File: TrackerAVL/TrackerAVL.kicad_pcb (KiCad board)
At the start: 2 copper layers, 120 x 80 mm, 173 parts, among them J801 Conn_02x07_Odd_Even, J802 Conn_01x15, J803 Conn_01x04, P201 uC_debug, Q201 DTC043ZEBTL, Q202 DTC043ZEBTL, Q203 DTC043ZEBTL, Q701 2N7002P, Q702 2N7002P, Q703 2N7002P, Q704 DTC043ZEBTL, U201 MAX3221, U202 LPC4337JBD144, U203 STS8C5H30L, U301 MPU-6050, U401 NAU8814, U501 STS8C5H30L, U502 LD1085D2T33R, U503 NCP114ASN180T1G, U601 MPCIE-Socket, U701 74LVC244APW, U801 74HC4053, X201 12MHz, X202 32.768K

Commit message: Cambios en pcb
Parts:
- moved C304 2.90 mm to (91.5, 36.8), turned to 0 degrees
- moved C303 1.94 mm to (79.6, 34.5)
- moved C301 1.91 mm to (79.6, 36.5)
- moved C401 1.58 mm to (134.9, 53.2)
- moved C402 1.56 mm to (134.9, 55.3)
- moved C403 1.55 mm to (134.9, 57.4)
- moved C404 1.51 mm to (134.9, 59.4)
- moved R406 1.15 mm to (149.2, 53.0)
- moved R408 1.13 mm to (149.2, 55.0)
- moved R407 1.13 mm to (149.2, 57.1)
- moved JP401 0.73 mm to (149.2, 49.1)
- moved C302 0.45 mm to (81.4, 30.2)
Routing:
- net /Audio/MICBIAS: track 25.4 -> 54.4 mm
- net +3V3: track 620.1 -> 641.9 mm, vias 78 -> 77
- net GND: track 487.1 -> 496.8 mm, vias 61 -> 60
- net /VBAT: track 102.5 -> 93.2 mm
- net +1V8: track 115.1 -> 121.7 mm
- net /Acelerómetro/INT: track 23.4 -> 27.4 mm
- net +BATT: track 13.0 -> 10.4 mm
- net Net-(R406-Pad1): track 4.71 -> 7.06 mm
- net Net-(C303-Pad1): track 2.49 -> 4.49 mm
- net /UC20_PCIe/I2C_SDA: track 38.9 -> 40.8 mm
- net /I2C_SCL: track 56.7 -> 58.5 mm
- net Net-(R403-Pad1): track 3.67 -> 5.38 mm
- net /I2C_SDA: track 59.6 -> 61.1 mm
- net Net-(R401-Pad1): track 3.96 -> 5.26 mm
- net /Audio/MICP: track 5.06 -> 6.22 mm
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
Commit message: Cambios en pcb
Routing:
- net GND: track 496.8 -> 497.7 mm, vias 60 -> 61

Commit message: Cambios en pcb
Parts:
- JP401: footprint Jumper:SolderJumper-2_P1.3mm_Bridged_Pad1.0x1.5mm -> NetTie:NetTie-2_SMD_Pad0.5mm
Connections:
- P201 pad 7: Net-(P201-Pad7) -> (no net)
- U201 pad 10: Net-(U201-Pad10) -> (no net)
- U202 pad 1: Net-(U202-Pad1) -> (no net)
- U202 pad 10: Net-(U202-Pad10) -> (no net)
- U202 pad 102: Net-(U202-Pad102) -> (no net)
- U202 pad 108: Net-(U202-Pad108) -> (no net)
- U202 pad 11: Net-(U202-Pad11) -> (no net)
- U202 pad 110: Net-(U202-Pad110) -> (no net)
- U202 pad 112: Net-(U202-Pad112) -> (no net)
- U202 pad 114: Net-(U202-Pad114) -> (no net)
- U202 pad 116: Net-(U202-Pad116) -> (no net)
- U202 pad 117: Net-(U202-Pad117) -> (no net)
- U202 pad 118: Net-(U202-Pad118) -> (no net)
- U202 pad 119: Net-(U202-Pad119) -> (no net)
- U202 pad 121: Net-(U202-Pad121) -> (no net)
- U202 pad 122: Net-(U202-Pad122) -> (no net)
- U202 pad 123: Net-(U202-Pad123) -> (no net)
- U202 pad 124: Net-(U202-Pad124) -> (no net)
- U202 pad 127: Net-(U202-Pad127) -> (no net)
- U202 pad 129: Net-(U202-Pad129) -> (no net)
- U202 pad 130: Net-(U202-Pad130) -> (no net)
- U202 pad 132: Net-(U202-Pad132) -> (no net)
- U202 pad 133: Net-(U202-Pad133) -> (no net)
- U202 pad 134: Net-(U202-Pad134) -> (no net)
- U202 pad 136: Net-(U202-Pad136) -> (no net)
- U202 pad 14: Net-(U202-Pad14) -> (no net)
- U202 pad 140: Net-(U202-Pad140) -> (no net)
- U202 pad 142: Net-(U202-Pad142) -> (no net)
- U202 pad 144: Net-(U202-Pad144) -> (no net)
- U202 pad 15: Net-(U202-Pad15) -> (no net)
- U202 pad 18: Net-(U202-Pad18) -> (no net)
- U202 pad 20: Net-(U202-Pad20) -> (no net)
- U202 pad 21: Net-(U202-Pad21) -> (no net)
- U202 pad 22: Net-(U202-Pad22) -> (no net)
- U202 pad 24: Net-(U202-Pad24) -> (no net)
- U202 pad 3: Net-(U202-Pad3) -> (no net)
- U202 pad 32: Net-(U202-Pad32) -> (no net)
- U202 pad 33: Net-(U202-Pad33) -> (no net)
- U202 pad 34: Net-(U202-Pad34) -> (no net)
- U202 pad 35: Net-(U202-Pad35) -> (no net)
- U202 pad 37: Net-(U202-Pad37) -> (no net)
- U202 pad 39: Net-(U202-Pad39) -> (no net)
- U202 pad 44: Net-(U202-Pad44) -> (no net)
- U202 pad 45: Net-(U202-Pad45) -> (no net)
- U202 pad 46: Net-(U202-Pad46) -> (no net)
- U202 pad 48: Net-(U202-Pad48) -> (no net)
- U202 pad 50: Net-(U202-Pad50) -> (no net)
- U202 pad 51: Net-(U202-Pad51) -> (no net)
- U202 pad 52: Net-(U202-Pad52) -> (no net)
- U202 pad 53: Net-(U202-Pad53) -> (no net)
- U202 pad 54: Net-(U202-Pad54) -> (no net)
- U202 pad 55: Net-(U202-Pad55) -> (no net)
- U202 pad 56: Net-(U202-Pad56) -> (no net)
- U202 pad 57: Net-(U202-Pad57) -> (no net)
- U202 pad 58: Net-(U202-Pad58) -> (no net)
- U202 pad 6: Net-(U202-Pad6) -> (no net)
- U202 pad 60: Net-(U202-Pad60) -> (no net)
- U202 pad 61: Net-(U202-Pad61) -> (no net)
- U202 pad 62: Net-(U202-Pad62) -> (no net)
- U202 pad 63: Net-(U202-Pad63) -> (no net)
- U202 pad 64: Net-(U202-Pad64) -> (no net)
- U202 pad 65: Net-(U202-Pad65) -> (no net)
- U202 pad 66: Net-(U202-Pad66) -> (no net)
- U202 pad 67: Net-(U202-Pad67) -> (no net)
- U202 pad 68: Net-(U202-Pad68) -> (no net)
- U202 pad 69: Net-(U202-Pad69) -> (no net)
- U202 pad 7: Net-(U202-Pad7) -> (no net)
- U202 pad 70: Net-(U202-Pad70) -> (no net)
- U202 pad 72: Net-(U202-Pad72) -> (no net)
- U202 pad 73: Net-(U202-Pad73) -> (no net)
- U202 pad 78: Net-(U202-Pad78) -> (no net)
- U202 pad 79: Net-(U202-Pad79) -> (no net)
- U202 pad 8: Net-(U202-Pad8) -> (no net)
- U202 pad 83: Net-(U202-Pad83) -> (no net)
- U202 pad 89: Net-(U202-Pad89) -> (no net)
- U202 pad 9: Net-(U202-Pad9) -> (no net)
- U202 pad 90: Net-(U202-Pad90) -> (no net)
- U202 pad 98: Net-(U202-Pad98) -> (no net)
- U202 pad 99: Net-(U202-Pad99) -> (no net)
- U301 pad 6: Net-(U301-Pad6) -> (no net)
- U301 pad 7: Net-(U301-Pad7) -> (no net)
- U401 pad 16: Net-(U401-Pad16) -> (no net)
- U401 pad 21: Net-(U401-Pad21) -> (no net)
- U601 pad 1: Net-(U601-Pad1) -> (no net)
- U601 pad 10: Net-(U601-Pad10) -> (no net)
- U601 pad 12: Net-(U601-Pad12) -> (no net)
- U601 pad 14: Net-(U601-Pad14) -> (no net)
- U601 pad 16: Net-(U601-Pad16) -> (no net)
- U601 pad 17: Net-(U601-Pad17) -> (no net)
- U601 pad 19: Net-(U601-Pad19) -> (no net)
- U601 pad 23: Net-(U601-Pad23) -> (no net)
- U601 pad 24: Net-(U601-Pad24) -> (no net)
- U601 pad 25: Net-(U601-Pad25) -> (no net)
- U601 pad 28: Net-(U601-Pad28) -> (no net)
- U601 pad 3: Net-(U601-Pad3) -> (no net)
- U601 pad 33: Net-(U601-Pad33) -> (no net)
- U601 pad 36: Net-(U601-Pad36) -> (no net)
- U601 pad 38: Net-(U601-Pad38) -> (no net)
- U601 pad 42: Net-(U601-Pad42) -> (no net)
- U601 pad 44: Net-(U601-Pad44) -> (no net)
- U601 pad 46: Net-(U601-Pad46) -> (no net)
- U601 pad 48: Net-(U601-Pad48) -> (no net)
- U601 pad 5: Net-(U601-Pad5) -> (no net)
- U601 pad 6: Net-(U601-Pad6) -> (no net)
- U601 pad 7: Net-(U601-Pad7) -> (no net)
- U601 pad 8: Net-(U601-Pad8) -> (no net)
- U701 pad 12: Net-(U701-Pad12) -> (no net)
- U701 pad 8: Net-(U701-Pad8) -> (no net)
- U801 pad 5: Net-(U801-Pad5) -> (no net)

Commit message: Últimos cambios en pcb
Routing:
- net GND: track 497.7 -> 495.1 mm, vias 61 -> 59
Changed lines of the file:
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@@
     (thickness 1.6)
     (drawings 30)
-    (tracks 2672)
+    (tracks 2670)
     (zones 0)
     (modules 173)
@@
   )
   (setup
-    (last_trace_width 0.25)
+    (last_trace_width 0.5)
     (user_trace_width 0.2)
     (user_trace_width 0.24)
@@
   (segment (start 101.475 67.275) (end 100.6 68.15) (width 0.25) (layer F.Cu) (net 1))
   (segment (start 100.6 71.125) (end 101.7 71.125) (width 0.5) (layer F.Cu) (net 1))
-  (segment (start 124.5 61.375) (end 124.5 59.22) (width 0.5) (layer F.Cu) (net 1))
+  (segment (start 124.5 61.375) (end 124.5 59.22) (width 0.25) (layer F.Cu) (net 1))
   (segment (start 121.475 69.355) (end 120.205 69.355) (width 0.5) (layer F.Cu) (net 1))
   (segment (start 121.475 67.85) (end 121.475 69.355) (width 0.5) (layer F.Cu) (net 1))
@@
   (via (at 120.5 43.55) (size 0.8) (drill 0.4) (layers F.Cu B.Cu) (net 1))
   (segment (start 120.5 45.15) (end 120.5 43.55) (width 0.5) (layer F.Cu) (net 1))
-  (via (at 149.1 61.25) (size 0.8) (drill 0.4) (layers F.Cu B.Cu) (net 1))
   (segment (start 149.1 59.275) (end 149.125 59.25) (width 0.5) (layer F.Cu) (net 1))
   (segment (start 149.1 61.25) (end 149.1 59.275) (width 0.5) (layer F.Cu) (net 1))
@@
   (segment (start 87.8 86.825) (end 90.875 86.825) (width 0.75) (layer F.Cu) (net 1))
   (via (at 133.9 61) (size 0.8) (drill 0.4) (layers F.Cu B.Cu) (net 1))
-  (via (at 149.9 51.425004) (size 0.8) (drill 0.4) (layers F.Cu B.Cu) (net 1))
-  (segment (start 149.9 51.990689) (end 149.9 51.425004) (width 0.5) (layer F.Cu) (net 1))
-  (segment (start 149.75 53.075) (end 149.9 52.925) (width 0.5) (layer F.Cu) (net 1))
-  (segment (start 149.9 52.925) (end 149.9 51.990689) (width 0.5) (layer F.Cu) (net 1))
-  (via (at 156.325 51.425) (size 0.8) (drill 0.4) (layers F.Cu B.Cu) (net 1))
-  (segment (start 149.9 51.425004) (end 156.324996 51.425004) (width 0.5) (layer B.Cu) (net 1))
-  (segment (start 156.324996 51.425004) (end 156.325 51.425) (width 0.5) (layer B.Cu) (net 1))
-  (via (at 156.3 61.225) (size 0.8) (drill 0.4) (layers F.Cu B.Cu) (net 1))
-  (segment (start 149.1 61.25) (end 156.275 61.25) (width 0.5) (layer B.Cu) (net 1))
-  (segment (start 156.275 61.25) (end 156.3 61.225) (width 0.5) (layer B.Cu) (net 1))
-  (segment (start 156.325 61.2) (end 156.3 61.225) (width 0.5) (layer F.Cu) (net 1))
-  (segment (start 156.325 51.425) (end 156.325 61.2) (width 0.5) (layer F.Cu) (net 1))
-  (segment (start 149.25 50.775004) (end 149.9 51.425004) (width 0.25) (layer F.Cu) (net 1))
-  (segment (start 149.25 49.8) (end 149.25 50.775004) (width 0.25) (layer F.Cu) (net 1))
   (segment (start 82.61486 34.58514) (end 82.324999 34.875001) (width 0.25) (layer F.Cu) (net 1))
   (segment (start 82.324999 34.875001) (end 81.925 35.275) (width 0.25) (layer F.Cu) (net 1))
@@
   (via (at 93.148372 35.15) (size 0.8) (drill 0.4) (layers F.Cu B.Cu) (net 1))
   (via (at 90.275 31.75) (size 0.8) (drill 0.4) (layers F.Cu B.Cu) (net 1))
+  (segment (start 55.2 61.55) (end 58.75 58) (width 0.5) (layer F.Cu) (net 1))
+  (segment (start 51.45 61.55) (end 55.2 61.55) (width 0.5) (layer F.Cu) (net 1))
+  (segment (start 149.875002 51.025001) (end 150.275001 51.425) (width 0.25) (layer F.Cu) (net 1))
+  (segment (start 149.25 50.399999) (end 149.875002 51.025001) (width 0.25) (layer F.Cu) (net 1))
+  (segment (start 149.25 49.8) (end 149.25 50.399999) (width 0.25) (layer F.Cu) (net 1))
+  (segment (start 150.225 51.475001) (end 150.275001 51.425) (width 0.5) (layer F.Cu) (net 1))
+  (segment (start 150.225 53.025) (end 150.225 51.475001) (width 0.5) (layer F.Cu) (net 1))
+  (via (at 150.275001 51.425) (size 0.8) (drill 0.4) (layers F.Cu B.Cu) (net 1))
+  (via (at 149.1 61.25) (size 0.8) (drill 0.4) (layers F.Cu B.Cu) (net 1))
+  (segment (start 150.675 51.824999) (end 150.275001 51.425) (width 0.5) (layer B.Cu) (net 1))
+  (segment (start 152.325001 53.475) (end 150.675 51.824999) (width 0.5) (layer B.Cu) (net 1))
+  (segment (start 152.325001 58.024999) (end 152.325001 53.475) (width 0.5) (layer B.Cu) (net 1))
+  (segment (start 149.1 61.25) (end 152.325001 58.024999) (width 0.5) (layer B.Cu) (net 1))
   (via (at 73 82) (size 0.8) (drill 0.4) (layers F.Cu B.Cu) (net 2))
   (via (at 71 82) (size 0.8) (drill 0.4) (layers F.Cu B.Cu) (net 2))
@@
   (via (at 90.90093 61.50093) (size 0.8) (drill 0.4) (layers F.Cu B.Cu) (net 15))
   (segment (start 90.90093 60.958216) (end 90.90093 61.50093) (width 0.24) (layer B.Cu) (net 15))
-  (segment (start 122.45 61.375) (end 120.5 61.375) (width 0.5) (layer F.Cu) (net 16))
+  (segment (start 122.45 61.375) (end 120.5 61.375) (width 0.25) (layer F.Cu) (net 16))
   (segment (start 116.7 60.3) (end 115.9 59.5) (width 0.25) (layer F.Cu) (net 16))
   (segment (start 120.5 60.3) (end 116.7 60.3) (width 0.25) (layer F.Cu) (net 16))
@@
   (segment (start 69.3 60) (end 69.1 59.8) (width 0.25) (layer F.Cu) (net 16))
   (segment (start 120.5 57.065) (end 122.45 57.065) (width 0.25) (layer F.Cu) (net 17))
-  (segment (start 122.45 57.065) (end 122.45 59.22) (width 0.5) (layer F.Cu) (net 17))
+  (segment (start 122.45 57.065) (end 122.45 59.22) (width 0.25) (layer F.Cu) (net 17))
   (via (at 69.3 61.1) (size 0.8) (drill 0.4) (layers F.Cu B.Cu) (net 17))
   (segment (start 67.925 61.1) (end 69.3 61.1) (width 0.25) (layer F.Cu) (net 17))
@@
   (segment (start 65.85 96.705) (end 62.905 96.705) (width 0.5) (layer F.Cu) (net 107))
   (segment (start 71.25 92.895) (end 71.25 94.165) (width 0.5) (layer F.Cu) (net 107))
-  (segment (start 70.225 94.165) (end 71.25 94.165) (width 0.25) (layer F.Cu) (net 107))
-  (segment (start 68.74 95.65) (end 70.225 94.165) (width 0.25) (layer F.Cu) (net 107))
-  (segment (start 65.85 96.705) (end 66.795 96.705) (width 0.25) (layer F.Cu) (net 107))
-  (segment (start 67.85 95.65) (end 68.74 95.65) (width 0.25) (layer F.Cu) (net 107))
-  (segment (start 66.795 96.705) (end 67.85 95.65) (width 0.25) (layer F.Cu) (net 107))
-  (segment (start 148.9 90.5) (end 150.45 88.95) (width 0.5) (layer F.Cu) (net 108))
-  (segment (start 147.4 90.5) (end 148.9 90.5) (width 0.5) (layer F.Cu) (net 108))
+  (segment (start 70.225 94.165) (end 71.25 94.165) (width 0.5) (layer F.Cu) (net 107))
+  (segment (start 68.74 95.65) (end 70.225 94.165) (width 0.5) (layer F.Cu) (net 107))
+  (segment (start 65.85 96.705) (end 66.795 96.705) (width 0.5) (layer F.Cu) (net 107))
+  (segment (start 67.85 95.65) (end 68.74 95.65) (width 0.5) (layer F.Cu) (net 107))
+  (segment (start 66.795 96.705) (end 67.85 95.65) (width 0.5) (layer F.Cu) (net 107))
+  (segment (start 148.9 90.5) (end 150.45 88.95) (width 0.25) (layer F.Cu) (net 108))
+  (segment (start 147.4 90.5) (end 148.9 90.5) (width 0.25) (layer F.Cu) (net 108))
   (via (at 150.4 80) (size 0.8) (drill 0.4) (layers F.Cu B.Cu) (net 108))
-  (segment (start 150.45 88.95) (end 150.45 80.05) (width 0.5) (layer F.Cu) (net 108))
+  (segment (start 150.45 88.95) (end 150.45 80.05) (width 0.25) (layer F.Cu) (net 108))
   (segment (start 150.45 80.05) (end 150.4 80) (width 0.5) (layer F.Cu) (net 108))
-  (segment (start 150.4 80) (end 149.9 79.5) (width 0.5) (layer B.Cu) (net 108))
+  (segment (start 150.4 80) (end 149.9 79.5) (width 0.25) (layer B.Cu) (net 108))
   (via (at 149.9 75.45) (size 0.8) (drill 0.4) (layers F.Cu B.Cu) (net 108))
-  (segment (start 149.9 79.5) (end 149.9 75.45) (width 0.5) (layer B.Cu) (net 108))
-  (segment (start 149.9 75.45) (end 149.9 72) (width 0.5) (layer F.Cu) (net 108))
-  (segment (start 146.875 68.975) (end 145.35 68.975) (width 0.5) (layer F.Cu) (net 108))
-  (segment (start 149.9 72) (end 146.875 68.975) (width 0.5) (layer F.Cu) (net 108))
+  (segment (start 149.9 79.5) (end 149.9 75.45) (width 0.25) (layer B.Cu) (net 108))
+  (segment (start 149.9 75.45) (end 149.9 72) (width 0.25) (layer F.Cu) (net 108))
+  (segment (start 146.875 68.975) (end 145.35 68.975) (width 0.25) (layer F.Cu) (net 108))
+  (segment (start 149.9 72) (end 146.875 68.975) (width 0.25) (layer F.Cu) (net 108))
   (segment (start 62.8 104.275) (end 64.87501 106.35001) (width 0.25) (layer F.Cu) (net 109))
   (segment (start 61.95 104.275) (end 62.8 104.275) (width 0.25) (layer F.Cu) (net 109))

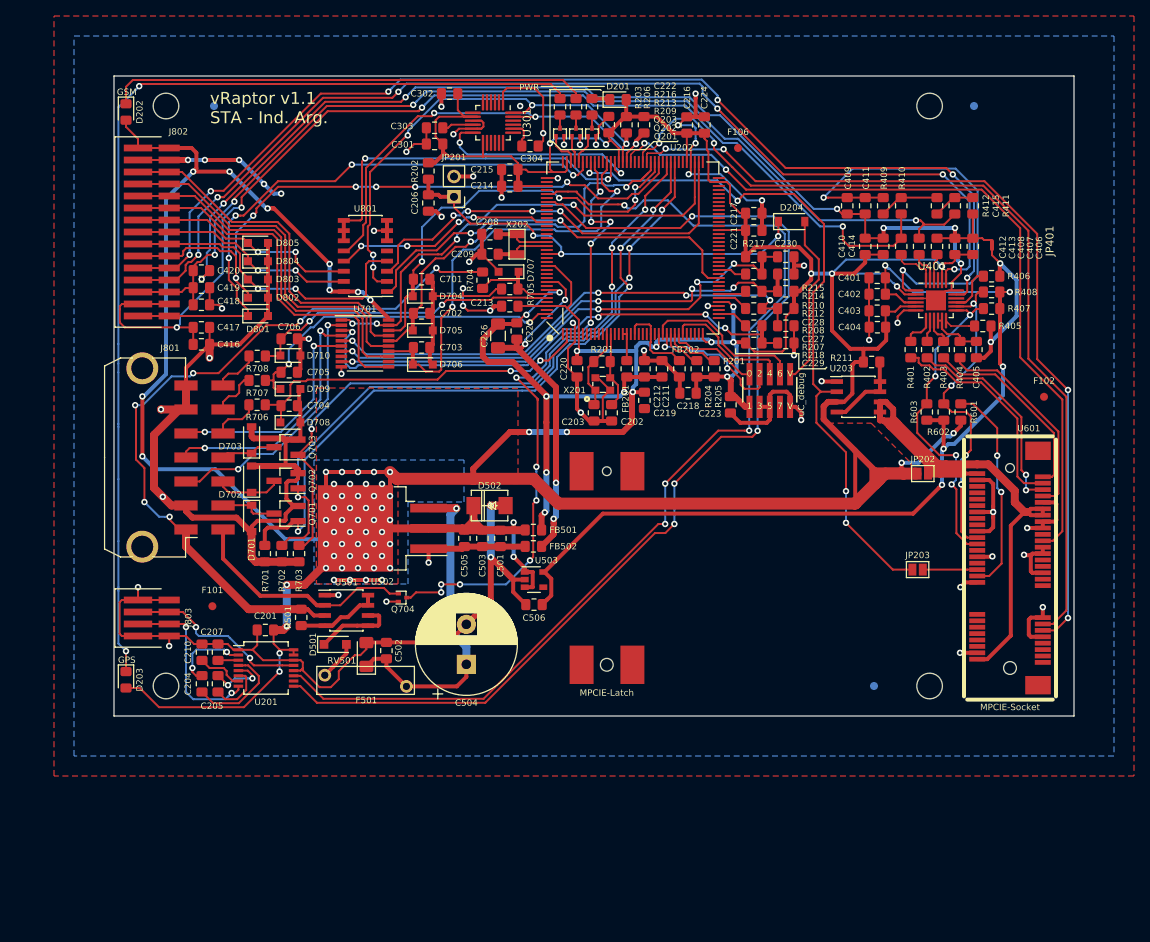
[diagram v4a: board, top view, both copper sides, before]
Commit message: Modificaciones varias
Se modifica acceso de pistas a pads (ahora a 90°).
Se agregan archivos de información al proyecto.
Se corrigen elementos 3d 24-QFN.
Modificaciones varias de pistas.
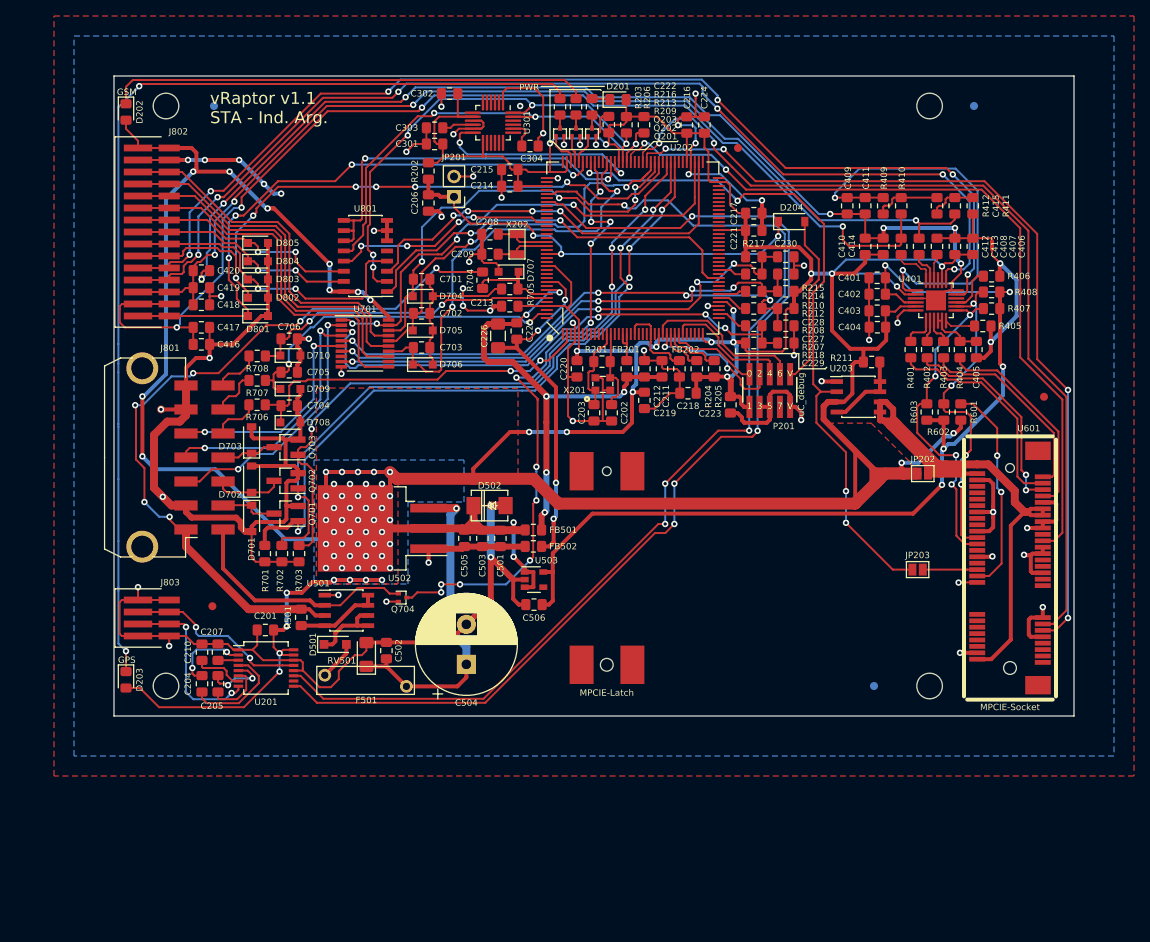
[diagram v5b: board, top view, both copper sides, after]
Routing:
- net GND: track 495.1 -> 507.3 mm
- net /Audio/MICBIAS: track 54.4 -> 51.9 mm
- net /CPU/DISPLAY_MODE: track 46.3 -> 48.7 mm
- net +3V3: track 641.9 -> 639.7 mm
- net /I2C_SCL: track 58.5 -> 59.7 mm
- net Net-(FB201-Pad2): track 3.82 -> 4.93 mm
- net /CPU/DIG_OUT_2: track 83.7 -> 84.8 mm
- net +1V8: track 121.7 -> 122.8 mm
- net Net-(C415-Pad1): track 7.57 -> 8.58 mm
- net +BATT: track 10.4 -> 9.51 mm
- net Net-(C415-Pad2): track 5.32 -> 6.22 mm
- net Net-(R204-Pad1): track 5.46 -> 6.25 mm
- net Net-(R205-Pad1): track 7.31 -> 8.09 mm
- net /SPI_SCK: track 28.0 -> 28.7 mm
- net /CPU/XTAL1: track 10.2 -> 11.0 mm
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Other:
- board text added: "A modificar en v1.2: > Modificar huellas para que posean el área que las delimita, así se valida el ERC en forma integral (con todos los checks activados). > Ver otros errores del ERC integral. > Ver posibilidad de que existan componentes en ambas capas. > Verificar diseño de v1.1 y corregir errores en caso de que existan."

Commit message: modificaciones en pcb
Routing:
- net GNDS: track 147.0 -> 149.7 mm, vias 7 -> 6
- net Net-(R405-Pad1): track 4.46 -> 5.39 mm
